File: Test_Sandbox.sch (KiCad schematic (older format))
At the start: 1 part

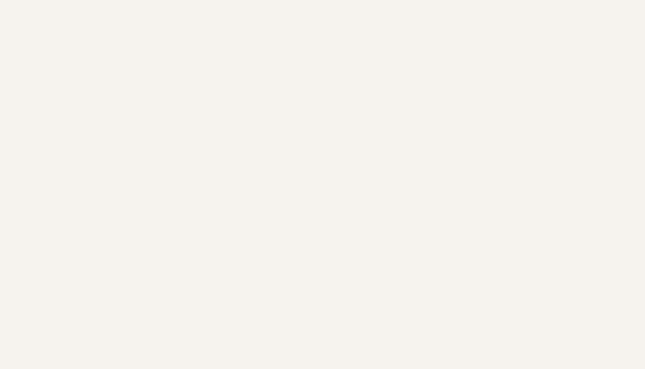
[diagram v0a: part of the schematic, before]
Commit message: added AMS1117-3.3 as voltage reference
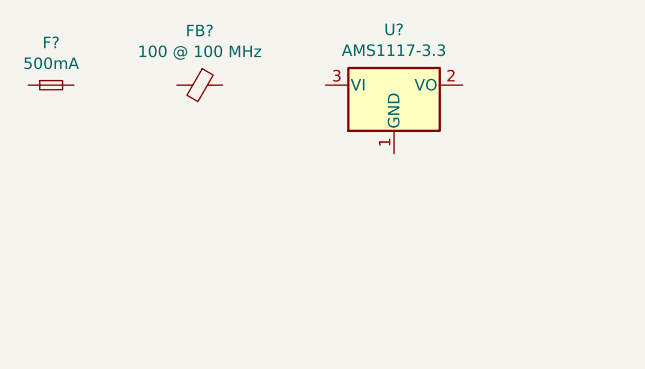
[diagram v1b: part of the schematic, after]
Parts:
- added F?: 500mA, symbol Device:Fuse_Small
- added FB?: 100 @ 100 MHz, symbol Device:Ferrite_Bead_Small
- added U?: AMS1117-3.3, Package_TO_SOT_SMD:SOT-223-3_TabPin2, symbol Regulator_Linear:AMS1117-3.3
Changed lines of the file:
@@
 EESchema Schematic File Version 4
+LIBS:Test_Sandbox-cache
 EELAYER 26 0
 EELAYER END
@@
 $EndComp
 NoConn ~ 7000 5100
+$Comp
+L Regulator_Linear:AMS1117-3.3 U?
+U 1 1 5F2CED56
+P 3100 1450
+F 0 "U?" H 3100 1692 50  0000 C CNN
+F 1 "AMS1117-3.3" H 3100 1601 50  0000 C CNN
+F 2 "Package_TO_SOT_SMD:SOT-223-3_TabPin2" H 3100 1650 50  0001 C CNN
+F 3 "http://www.advanced-monolithic.com/pdf/ds1117.pdf" H 3200 1200 50  0001 C CNN
+	1    3100 1450
+	1    0    0    -1
+$EndComp
+$Comp
+L Device:Ferrite_Bead_Small FB?
+U 1 1 5F2CEE95
+P 2250 1450
+F 0 "FB?" V 2013 1450 50  0000 C CNN
+F 1 "100 @ 100 MHz" V 2104 1450 50  0000 C CNN
+F 2 "" V 2180 1450 50  0001 C CNN
+F 3 "~" H 2250 1450 50  0001 C CNN
+	1    2250 1450
+	0    1    1    0
+$EndComp
+$Comp
+L Device:Fuse_Small F?
+U 1 1 5F2CEF1D
+P 1600 1450
+F 0 "F?" H 1600 1635 50  0000 C CNN
+F 1 "500mA" H 1600 1544 50  0000 C CNN
+F 2 "" H 1600 1450 50  0001 C CNN
+F 3 "~" H 1600 1450 50  0001 C CNN
+	1    1600 1450
+	1    0    0    -1
+$EndComp
 $EndSCHEMATC

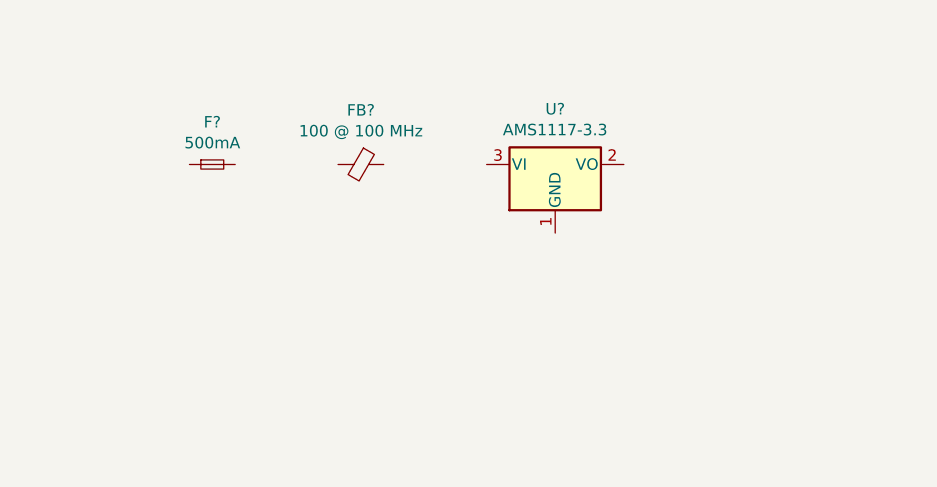
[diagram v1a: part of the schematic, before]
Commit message: Completed input voltage regulator section
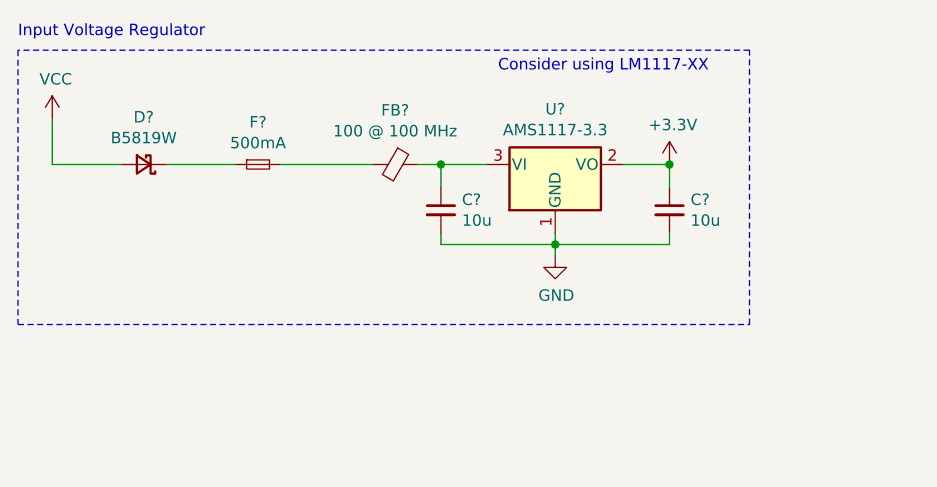
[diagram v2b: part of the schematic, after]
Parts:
- added C? (x2): 10u, symbol Device:C_Small
- added D?: B5819W, symbol Device:D_Schottky_Small
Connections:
- net GND: now reaches U?.1 (GND)
- net GND: now also C?.2, C?.2
- net +3V3: now reaches U?.2 (VO)
- net +3V3: now also C?.1
- net at U?.3 (VI): now also FB?.1, C?.1
- net at FB?.2: now also F?.2
- net at F?.1: now also D?.1 (K)
- new net VCC: D?.2 (A)
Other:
- note added: "Consider using LM1117-XX"
- note added: "Input Voltage Regulator"
- moved on the sheet: F?, FB?
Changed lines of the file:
@@
 EESchema Schematic File Version 4
-LIBS:Test_Sandbox-cache
-EELAYER 26 0
+EELAYER 30 0
 EELAYER END
 $Descr A4 11693 8268
@@
 L Device:Ferrite_Bead_Small FB?
 U 1 1 5F2CEE95
-P 2250 1450
-F 0 "FB?" V 2013 1450 50  0000 C CNN
-F 1 "100 @ 100 MHz" V 2104 1450 50  0000 C CNN
-F 2 "" V 2180 1450 50  0001 C CNN
-F 3 "~" H 2250 1450 50  0001 C CNN
-	1    2250 1450
+P 2400 1450
+F 0 "FB?" V 2163 1450 50  0000 C CNN
+F 1 "100 @ 100 MHz" V 2254 1450 50  0000 C CNN
+F 2 "" V 2330 1450 50  0001 C CNN
+F 3 "~" H 2400 1450 50  0001 C CNN
+	1    2400 1450
 	0    1    1    0
 $EndComp
@@
 L Device:Fuse_Small F?
 U 1 1 5F2CEF1D
-P 1600 1450
-F 0 "F?" H 1600 1635 50  0000 C CNN
-F 1 "500mA" H 1600 1544 50  0000 C CNN
-F 2 "" H 1600 1450 50  0001 C CNN
-F 3 "~" H 1600 1450 50  0001 C CNN
-	1    1600 1450
+P 1800 1450
+F 0 "F?" H 1800 1635 50  0000 C CNN
+F 1 "500mA" H 1800 1544 50  0000 C CNN
+F 2 "" H 1800 1450 50  0001 C CNN
+F 3 "~" H 1800 1450 50  0001 C CNN
+	1    1800 1450
 	1    0    0    -1
 $EndComp
+$Comp
+L Device:D_Schottky_Small D?
+U 1 1 5F3CB856
+P 1300 1450
+F 0 "D?" H 1300 1243 50  0000 C CNN
+F 1 "B5819W" H 1300 1334 50  0000 C CNN
+F 2 "" V 1300 1450 50  0001 C CNN
+F 3 "~" V 1300 1450 50  0001 C CNN
+	1    1300 1450
+	-1   0    0    1
+$EndComp
+Wire Wire Line
+	1400 1450 1700 1450
+Wire Wire Line
+	1900 1450 2300 1450
+Wire Wire Line
+	2500 1450 2600 1450
+$Comp
+L Device:C_Small C?
+U 1 1 5F3CF384
+P 2600 1650
+F 0 "C?" H 2692 1696 50  0000 L CNN
+F 1 "10u" H 2692 1605 50  0000 L CNN
+F 2 "" H 2600 1650 50  0001 C CNN
+F 3 "~" H 2600 1650 50  0001 C CNN
+	1    2600 1650
+	1    0    0    -1
+$EndComp
+$Comp
+L Device:C_Small C?
+U 1 1 5F3CFB72
+P 3600 1650
+F 0 "C?" H 3692 1696 50  0000 L CNN
+F 1 "10u" H 3692 1605 50  0000 L CNN
+F 2 "" H 3600 1650 50  0001 C CNN
+F 3 "~" H 3600 1650 50  0001 C CNN
+	1    3600 1650
+	1    0    0    -1
+$EndComp
+Wire Wire Line
+	2600 1550 2600 1450
+Connection ~ 2600 1450
+Wire Wire Line
+	2600 1450 2800 1450
+$Comp
+L power:GND #PWR?
+U 1 1 5F3D06C5
+P 3100 1850
+F 0 "#PWR?" H 3100 1600 50  0001 C CNN
+F 1 "GND" H 3105 1677 50  0000 C CNN
+F 2 "" H 3100 1850 50  0001 C CNN
+F 3 "" H 3100 1850 50  0001 C CNN
+	1    3100 1850
+	1    0    0    -1
+$EndComp
+Wire Wire Line
+	3100 1750 3100 1800
+Wire Wire Line
+	2600 1750 2600 1800
+Wire Wire Line
+	2600 1800 3100 1800
+Connection ~ 3100 1800
+Wire Wire Line
+	3100 1800 3100 1850
+Wire Wire Line
+	3400 1450 3600 1450
+Wire Wire Line
+	3600 1450 3600 1550
+Wire Wire Line
+	3600 1750 3600 1800
+Wire Wire Line
+	3600 1800 3100 1800
+$Comp
+L power:VCC #PWR?
+U 1 1 5F3D45A1
+P 900 1250
+F 0 "#PWR?" H 900 1100 50  0001 C CNN
+F 1 "VCC" H 915 1423 50  0000 C CNN
+F 2 "" H 900 1250 50  0001 C CNN
+F 3 "" H 900 1250 50  0001 C CNN
+	1    900  1250
+	1    0    0    -1
+$EndComp
+Wire Wire Line
+	900  1250 900  1450
+Wire Wire Line
+	900  1450 1200 1450
+$Comp
+L power:+3.3V #PWR?
+U 1 1 5F3D4D83
+P 3600 1450
+F 0 "#PWR?" H 3600 1300 50  0001 C CNN
+F 1 "+3.3V" H 3615 1623 50  0000 C CNN
+F 2 "" H 3600 1450 50  0001 C CNN
+F 3 "" H 3600 1450 50  0001 C CNN
+	1    3600 1450
+	1    0    0    -1
+$EndComp
+Connection ~ 3600 1450
+Wire Notes Line
+	750  2150 3950 2150
+Wire Notes Line
+	3950 2150 3950 950
+Wire Notes Line
+	3950 950  750  950
+Wire Notes Line
+	750  950  750  2150
+Text Notes 750  900  0    50   ~ 0
+Input Voltage Regulator
+Text Notes 2850 1050 0    50   ~ 0
+Consider using LM1117-XX
 $EndSCHEMATC
